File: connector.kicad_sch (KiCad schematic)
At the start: 2 parts, among them J401 AXK500137YG, J402 AXK500137YG

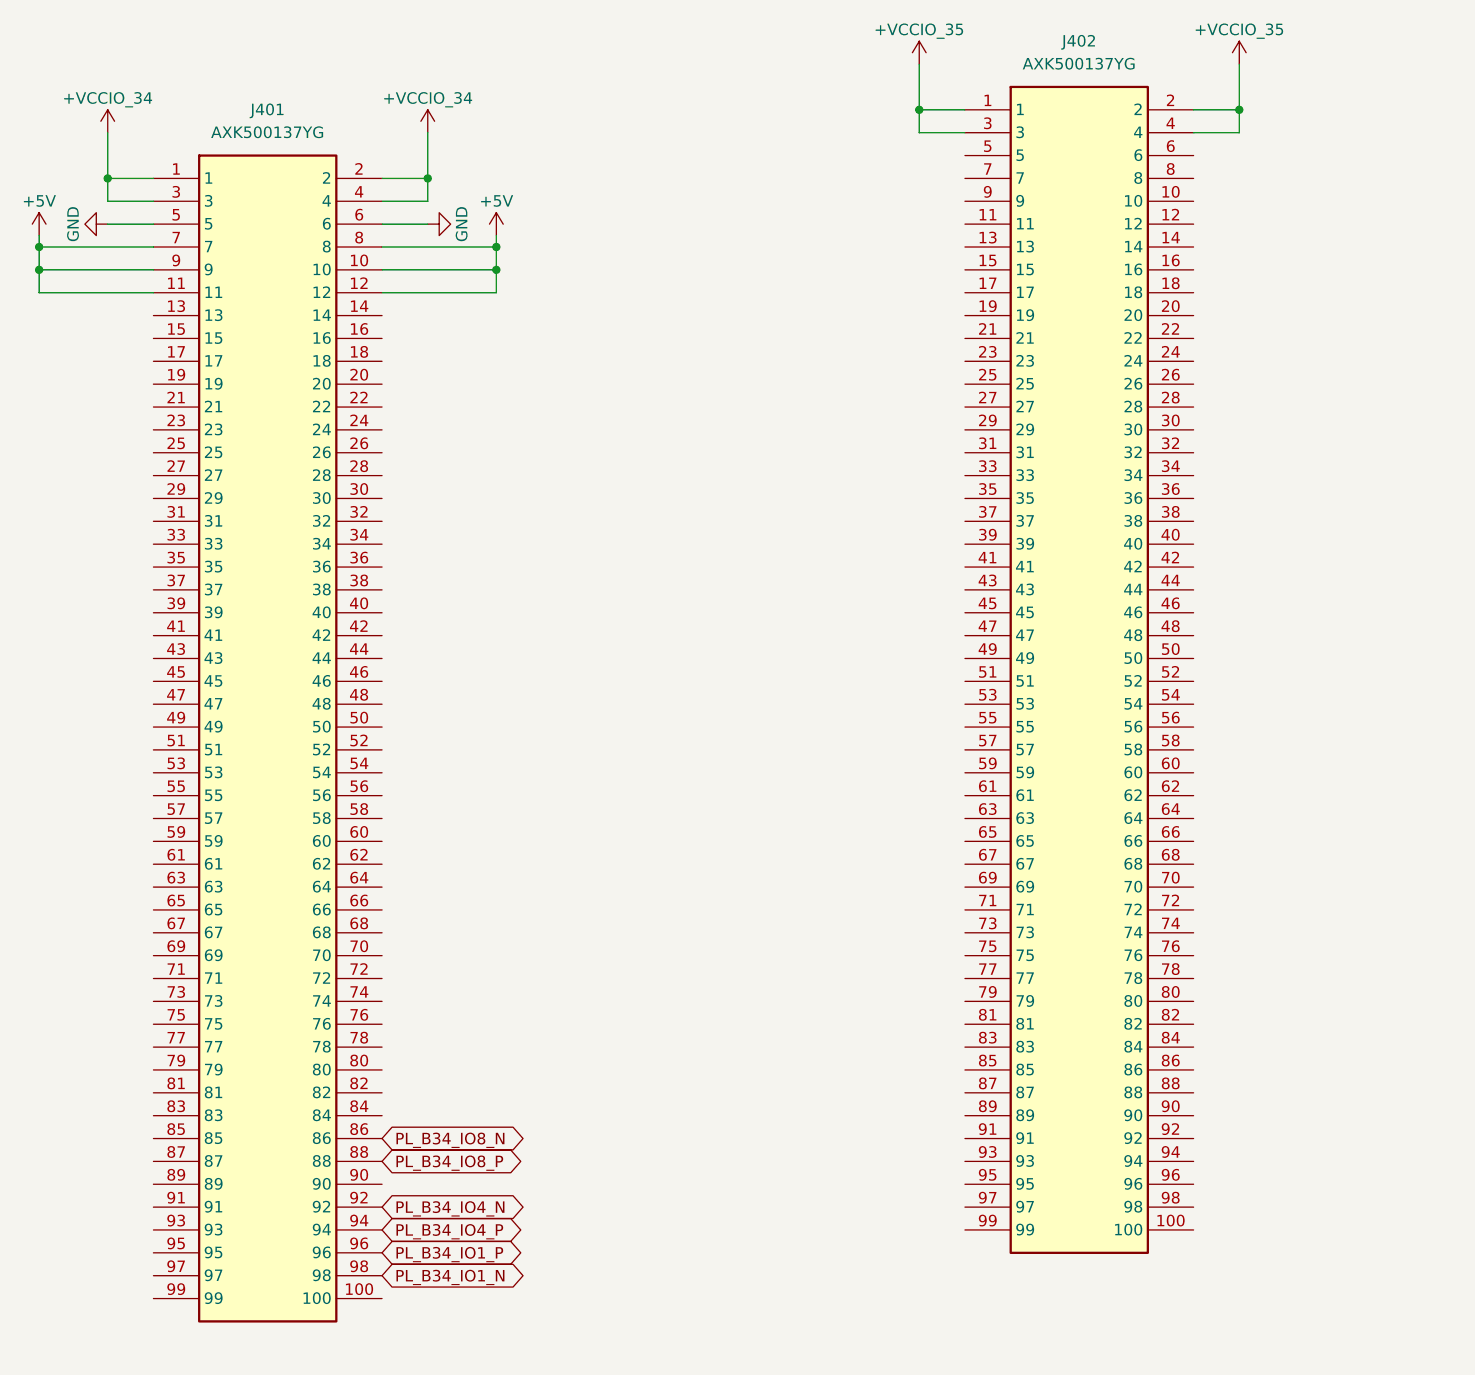
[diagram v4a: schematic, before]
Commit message: layout: route mio and some io
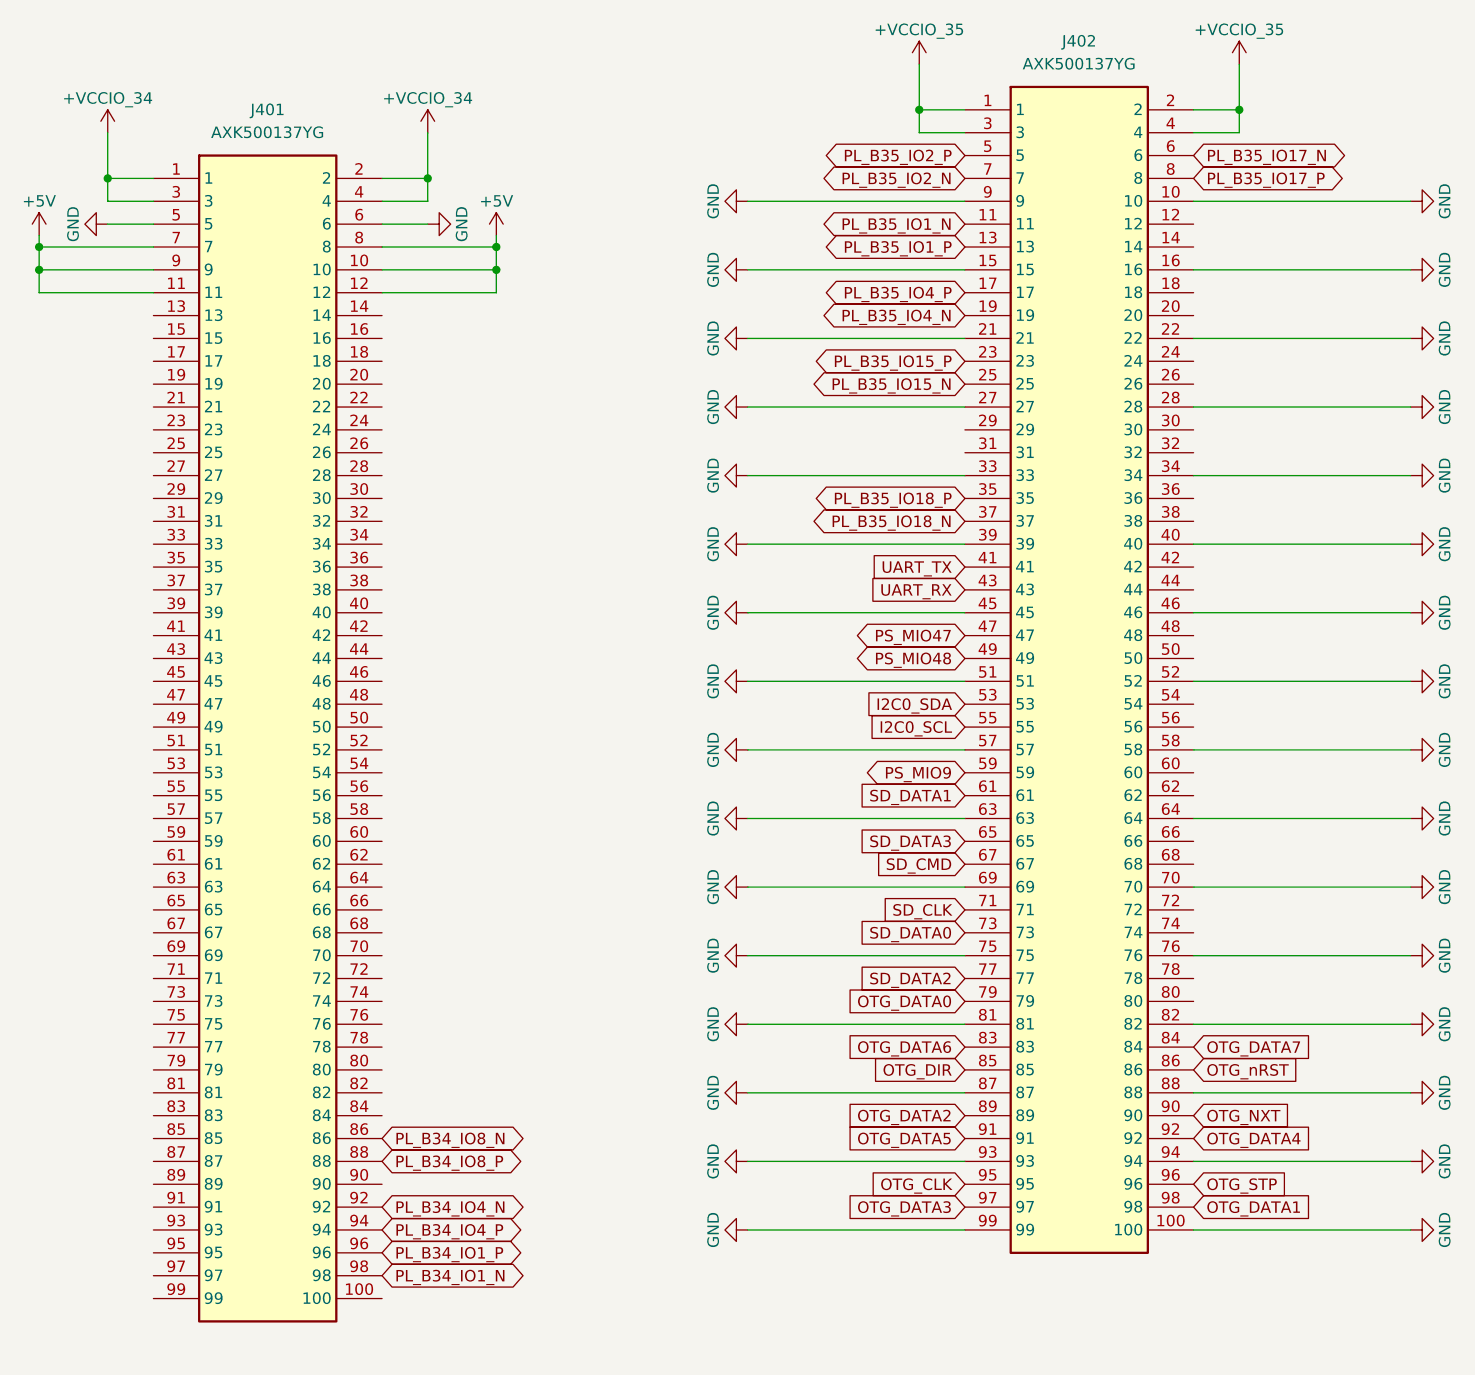
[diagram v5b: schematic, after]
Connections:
- net GND: now also J402.10, J402.100, J402.15, J402.16, J402.21, J402.22, J402.27, J402.28, J402.33, J402.34, J402.39, J402.40, J402.45, J402.46, J402.51, J402.52, J402.57, J402.58, J402.63, J402.64, J402.69, J402.70, J402.75, J402.76, J402.81, J402.82, J402.87, J402.88, J402.9, J402.93, J402.94, J402.99
- net PL_B35_IO1_N: now reaches J402.11
- net PL_B35_IO1_P: now reaches J402.13
- net PL_B35_IO4_P: now reaches J402.17
- net PL_B35_IO4_N: now reaches J402.19
- net PL_B35_IO15_P: now reaches J402.23
- net PL_B35_IO15_N: now reaches J402.25
- net PL_B35_IO18_P: now reaches J402.35
- net PL_B35_IO18_N: now reaches J402.37
- net UART_TX: now reaches J402.41
- net UART_RX: now reaches J402.43
- net PS_MIO47: now reaches J402.47
- net PS_MIO48: now reaches J402.49
- net PL_B35_IO2_P: now reaches J402.5
- net I2C0_SDA: now reaches J402.53
- net I2C0_SCL: now reaches J402.55
- net PS_MIO9: now reaches J402.59
- net PL_B35_IO17_N: now reaches J402.6
- net SD_DATA1: now reaches J402.61
- net SD_DATA3: now reaches J402.65
- net SD_CMD: now reaches J402.67
- net PL_B35_IO2_N: now reaches J402.7
- net SD_CLK: now reaches J402.71
- net SD_DATA0: now reaches J402.73
- net SD_DATA2: now reaches J402.77
- net OTG_DATA0: now reaches J402.79
- net PL_B35_IO17_P: now reaches J402.8
- net OTG_DATA6: now reaches J402.83
- net OTG_DATA7: now reaches J402.84
- net OTG_DIR: now reaches J402.85
- net OTG_nRST: now reaches J402.86
- net OTG_DATA2: now reaches J402.89
- net OTG_NXT: now reaches J402.90
- net OTG_DATA5: now reaches J402.91
- net OTG_DATA4: now reaches J402.92
- net OTG_CLK: now reaches J402.95
- net OTG_STP: now reaches J402.96
- net OTG_DATA3: now reaches J402.97
- net OTG_DATA1: now reaches J402.98
